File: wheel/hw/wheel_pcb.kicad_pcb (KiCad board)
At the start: 2 copper layers, 36 x 67 mm, 50 parts, among them J2 DEBUG, J3 IO_C, J4 CAR, J5 IO_B, J6 IO_A, SW1 CONFIG, U1 LPC11C24FBD48, U2 TPS62175, U3 TLV70233_SOT23-5, Y1 12MHz

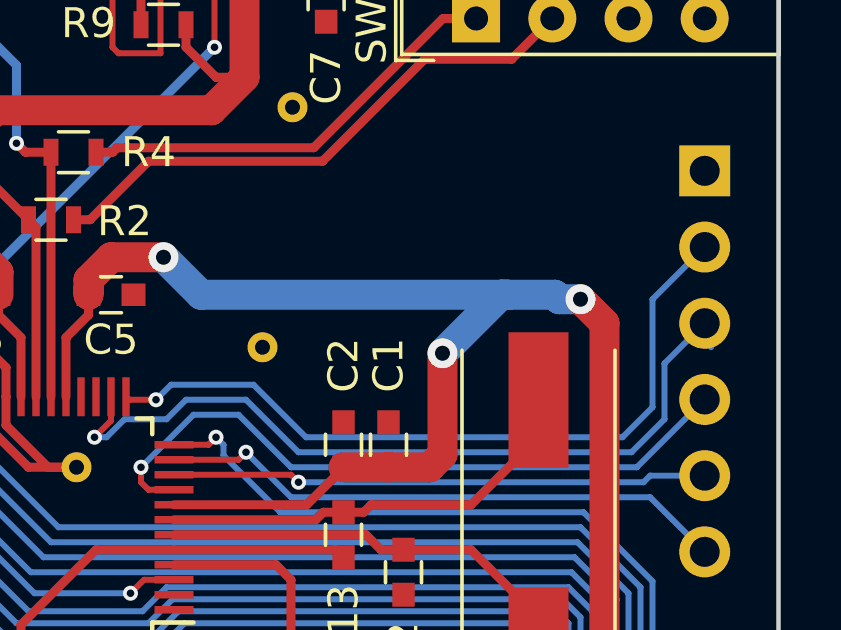
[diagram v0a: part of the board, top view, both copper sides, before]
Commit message: remove stray track and clean up tracks
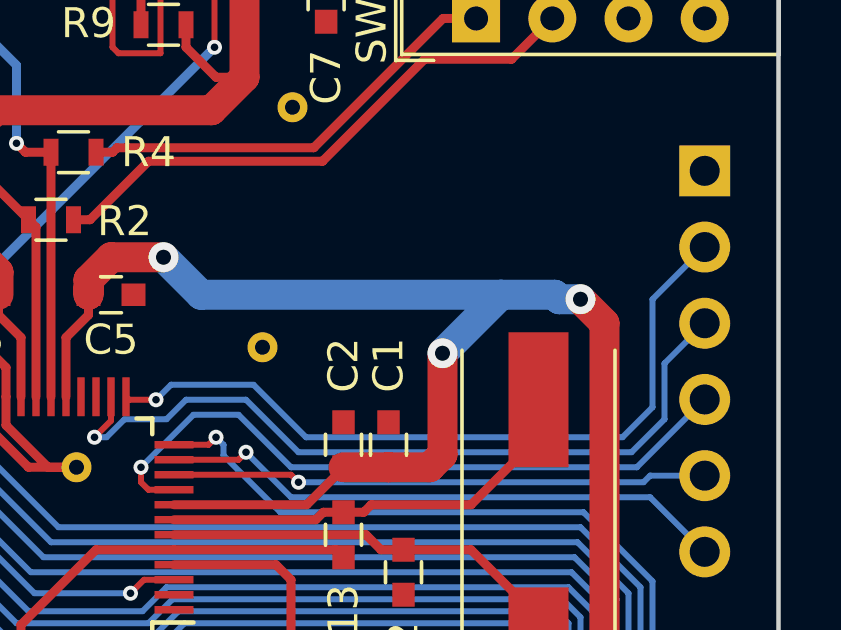
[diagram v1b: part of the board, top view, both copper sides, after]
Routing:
- net /IO_C2: track 26.9 -> 26.0 mm
- net +3V3: track 145.3 -> 144.8 mm
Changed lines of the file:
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@@
     (links 120)
     (no_connects 0)
-    (area 222.924999 54.924999 259.075001 122.075001)
+    (area 217.492857 54.924999 261.045 123.025)
     (thickness 1.6)
     (drawings 11)
-    (tracks 404)
+    (tracks 402)
     (zones 0)
     (modules 50)
@@
     (pcbplotparams
       (layerselection 0x010f0_80000001)
-      (usegerberextensions false)
+      (usegerberextensions true)
       (excludeedgelayer true)
       (linewidth 0.100000)
@@
       (drillshape 0)
       (scaleselection 1)
-      (outputdirectory ""))
+      (outputdirectory r1/))
   )
   (net 0 "")
@@
   (segment (start 247.8 80.575) (end 247.375 81) (width 1) (layer F.Cu) (net 3))
   (segment (start 247.8 77.2) (end 249.75 75.25) (width 1) (layer B.Cu) (net 3))
-  (segment (start 249.75 75.25) (end 250 75.25) (width 1) (layer B.Cu) (net 3))
+  (segment (start 249.75 75.25) (end 239.75 75.25) (width 1) (layer B.Cu) (net 3))
   (segment (start 245 96.15) (end 245 93) (width 1) (layer F.Cu) (net 3) (status 10))
   (segment (start 245 93) (end 242.75 90.75) (width 1) (layer F.Cu) (net 3))
@@
   (segment (start 236 75.25) (end 236 74.75) (width 1) (layer F.Cu) (net 3) (status 10))
   (segment (start 236 75) (end 236 75.25) (width 1) (layer F.Cu) (net 3) (status 30))
-  (segment (start 250 75.25) (end 239.75 75.25) (width 1) (layer B.Cu) (net 3))
   (segment (start 239.75 75.25) (end 238.5 74) (width 1) (layer B.Cu) (net 3))
   (via (at 238.5 74) (size 1) (drill 0.5) (layers F.Cu B.Cu) (net 3))
@@
   (segment (start 244.5 81) (end 244.5 80.975) (width 0.5) (layer F.Cu) (net 3) (status 30))
   (segment (start 242 90) (end 242.75 90.75) (width 1) (layer B.Cu) (net 3))
-  (segment (start 232.75 87.35) (end 232.75 88.3) (width 0.3) (layer F.Cu) (net 4))
+  (segment (start 232.75 87.35) (end 232.75 88.3) (width 0.3) (layer F.Cu) (net 4) (status 10))
   (segment (start 232.75 88.3) (end 232.45 88.6) (width 0.3) (layer F.Cu) (net 4))
   (segment (start 232.45 88.6) (end 231.4 88.6) (width 0.3) (layer F.Cu) (net 4))
@@
   (segment (start 230.2 88) (end 227.4 90.8) (width 0.3) (layer F.Cu) (net 4))
   (segment (start 227.4 90.8) (end 227.4 93.65) (width 0.3) (layer F.Cu) (net 4))
-  (segment (start 227.4 93.65) (end 226.6 94.45) (width 0.3) (layer F.Cu) (net 4))
-  (segment (start 226.6 94.45) (end 226.4 94.45) (width 0.3) (layer F.Cu) (net 4))
+  (segment (start 227.4 93.65) (end 226.6 94.45) (width 0.3) (layer F.Cu) (net 4) (status 20))
+  (segment (start 226.6 94.45) (end 226.4 94.45) (width 0.3) (layer F.Cu) (net 4) (status 30))
   (segment (start 226.4 93.8) (end 225.65 93.8) (width 0.3) (layer F.Cu) (net 5))
-  (segment (start 225.65 93.8) (end 225 94.45) (width 0.3) (layer F.Cu) (net 5))
-  (segment (start 225 94.45) (end 224.8 94.45) (width 0.3) (layer F.Cu) (net 5))
+  (segment (start 225.65 93.8) (end 225 94.45) (width 0.3) (layer F.Cu) (net 5) (status 20))
+  (segment (start 225 94.45) (end 224.8 94.45) (width 0.3) (layer F.Cu) (net 5) (status 30))
   (segment (start 226.8 93.4) (end 226.4 93.8) (width 0.3) (layer F.Cu) (net 5))
   (segment (start 226.8 90.4) (end 226.8 93.4) (width 0.3) (layer F.Cu) (net 5))
@@
   (via (at 237.4 85.2) (size 0.5) (drill 0.25) (layers F.Cu B.Cu) (net 37))
   (segment (start 247.2 67.4) (end 250.1 67.4) (width 0.3) (layer F.Cu) (net 38))
-  (segment (start 250.1 67.4) (end 251.46 66.04) (width 0.3) (layer F.Cu) (net 38))
+  (segment (start 250.1 67.4) (end 251.46 66.04) (width 0.3) (layer F.Cu) (net 38) (status 20))
   (segment (start 238 70.8) (end 243.8 70.8) (width 0.3) (layer F.Cu) (net 38))
   (segment (start 243.8 70.8) (end 247.2 67.4) (width 0.3) (layer F.Cu) (net 38))
   (segment (start 236.05 72.75) (end 238 70.8) (width 0.3) (layer F.Cu) (net 38))
-  (segment (start 235.5 72.75) (end 236.05 72.75) (width 0.3) (layer F.Cu) (net 38))
+  (segment (start 235.5 72.75) (end 236.05 72.75) (width 0.3) (layer F.Cu) (net 38) (status 10))
   (segment (start 235.5 72.75) (end 235.5 72.55) (width 0.3) (layer F.Cu) (net 38) (status 30))
-  (segment (start 247.82 66.04) (end 248.92 66.04) (width 0.3) (layer F.Cu) (net 39))
+  (segment (start 247.82 66.04) (end 248.92 66.04) (width 0.3) (layer F.Cu) (net 39) (status 20))
   (segment (start 243.510009 70.349991) (end 247.82 66.04) (width 0.3) (layer F.Cu) (net 39))
   (segment (start 236.950009 70.349991) (end 243.510009 70.349991) (width 0.3) (layer F.Cu) (net 39))
   (segment (start 236.8 70.5) (end 236.950009 70.349991) (width 0.3) (layer F.Cu) (net 39))
-  (segment (start 236.25 70.5) (end 236.8 70.5) (width 0.3) (layer F.Cu) (net 39))
+  (segment (start 236.25 70.5) (end 236.8 70.5) (width 0.3) (layer F.Cu) (net 39) (status 10))
   (segment (start 236.25 70.5) (end 236.25 70.7) (width 0.3) (layer F.Cu) (net 39) (status 30))
   (segment (start 238.25 78.75) (end 238.75 78.25) (width 0.2) (layer B.Cu) (net 44))
@@
   (segment (start 255.2 77.54) (end 256.54 76.2) (width 0.2) (layer B.Cu) (net 45) (status 20))
   (via (at 236.2 80) (size 0.5) (drill 0.25) (layers F.Cu B.Cu) (net 45))
-  (segment (start 256.75 77) (end 256.75 76.127919) (width 0.2) (layer B.Cu) (net 45) (status 30))
   (segment (start 237.75 81) (end 239.5 79.25) (width 0.2) (layer B.Cu) (net 46))
   (segment (start 239.5 79.25) (end 241 79.25) (width 0.2) (layer B.Cu) (net 46))

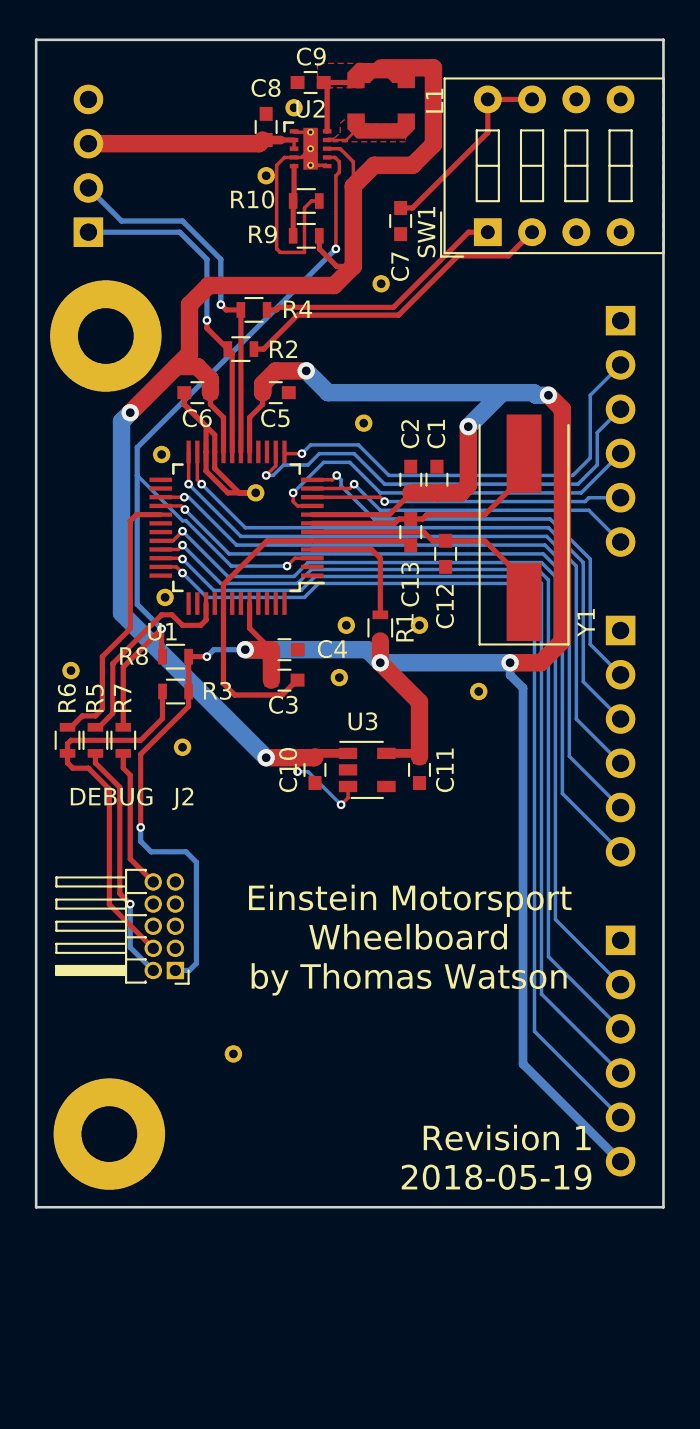
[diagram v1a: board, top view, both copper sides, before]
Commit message: draft layout of new wheel stuff
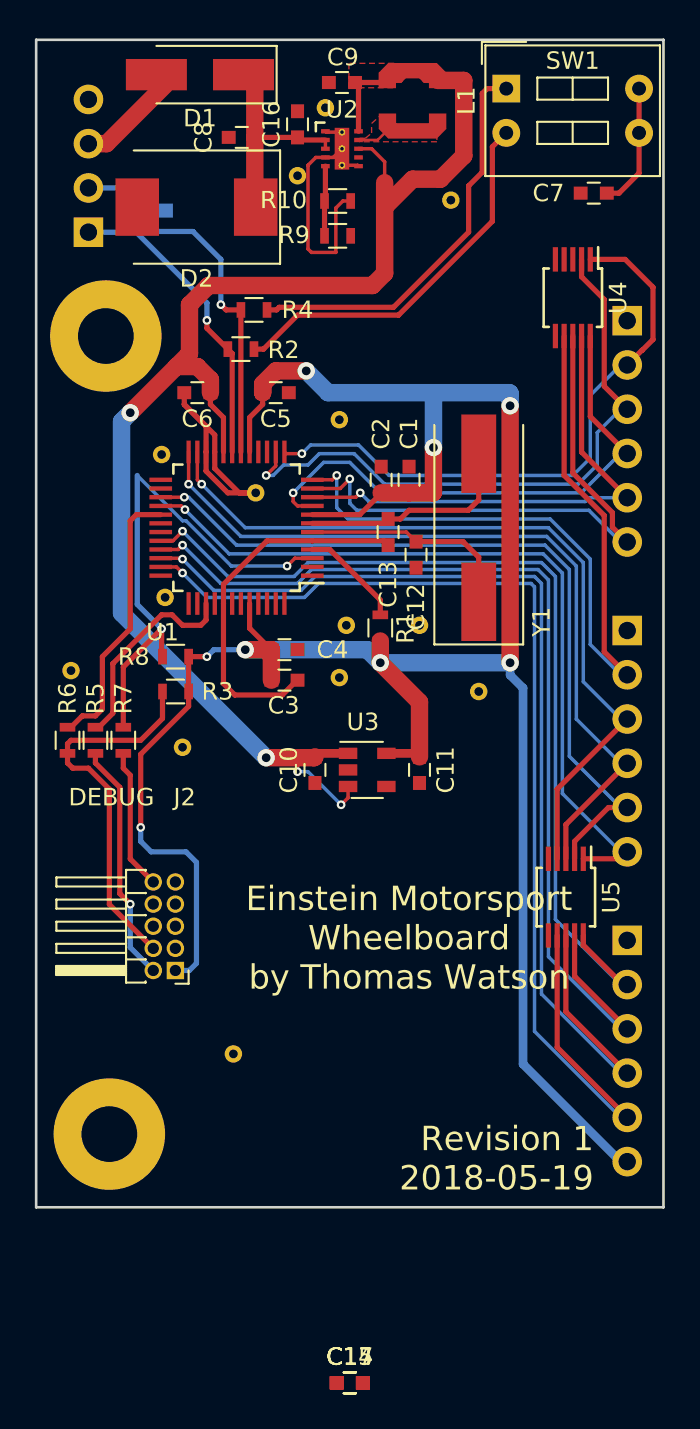
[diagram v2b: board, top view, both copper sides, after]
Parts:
- added C14, C15, C17: 100n, Capacitors_SMD:C_0603, F.Cu at (241.0, 132.1)
- added C16: 100n, Capacitors_SMD:C_0603, F.Cu at (238.0, 59.9)
- added D1: SS14, Diodes_SMD:D_SMA_Handsoldering, F.Cu at (232.4, 57.0)
- added D2: SMLJ22A-Q, Diodes_SMD:D_SMC, F.Cu at (232.2, 64.6)
- added D3: PESD1CAN-U, TO_SOT_Packages_SMD:SOT-23, B.Cu at (229.4, 64.8)
- added U4: SP4065-08ATG, Housings_SSOP:MSOP-10_3x3mm_Pitch0.5mm, F.Cu at (253.8, 69.8)
- added U5: SP4065-08ATG, Housings_SSOP:MSOP-10_3x3mm_Pitch0.5mm, F.Cu at (253.4, 104.2)
- R2, R4: value 60.4 -> 62
- R5, R6, R7: value 60.4 -> 100
- SW1: value CONFIG -> TERM; footprint Buttons_Switches_THT:SW_DIP_x4_W7.62mm_Slide -> Buttons_Switches_THT:SW_DIP_x2_W7.62mm_Slide
- moved C7 11.2 mm to (255.0, 63.8), turned to 180 degrees
- moved SW1 8.31 mm to (250.0, 57.8), turned to 0 degrees
- moved REF** 6.25 mm to (246.8, 64.2)
- moved Y1 2.60 mm to (248.4, 83.0)
- moved C9 1.80 mm to (240.6, 57.5)
- moved R10 1.80 mm to (240.3, 64.2)
- moved R9 1.80 mm to (240.3, 66.2)
- moved REF** 1.80 mm to (238.0, 62.8)
- moved U2 1.80 mm to (240.6, 61.2)
- moved L1 1.80 mm to (244.6, 58.5)
- moved REF** 1.80 mm to (239.6, 58.9)
- moved C12 1.70 mm to (244.8, 84.5)
- moved C2 1.70 mm to (242.8, 80.2)
- moved C1 1.60 mm to (244.4, 80.2)
- moved C8 1.52 mm to (234.8, 60.6), turned to 180 degrees
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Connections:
- C8 pad 1: +BATT -> Net-(C16-Pad1)
- SW1 pad 3: Net-(SW1-Pad3) -> Net-(C7-Pad1)
- SW1 pad 4: Net-(SW1-Pad4) -> Net-(C7-Pad1)
- U2 pad 2: +BATT -> Net-(C16-Pad1)
- U2 pad 3: +BATT -> Net-(C16-Pad1)
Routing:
- net /MCU_~RESET: track 53.6 -> 30.0 mm, vias 3 -> 2
- net /IO_B1: track 25.6 -> 47.4 mm
- net Net-(C16-Pad1): track 0.00 -> 14.5 mm
- net /IO_C5: track 19.2 -> 33.4 mm
- net /IO_A4: track 55.1 -> 67.2 mm
- net /IO_C4: track 17.9 -> 28.5 mm
- net /IO_C2: track 26.0 -> 35.7 mm
- net /IO_B2: track 35.6 -> 45.3 mm
- net /IO_A3: track 53.1 -> 62.5 mm
- net /IO_C1: track 25.0 -> 34.3 mm
- net /CANL_TERM: track 14.7 -> 23.4 mm
- net /IO_C3: track 22.9 -> 30.5 mm
- net +3V3: track 144.8 -> 137.5 mm
- net /IO_B3: track 38.4 -> 45.4 mm
- net /IO_A2: track 51.3 -> 57.9 mm
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
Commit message: rework some tracks
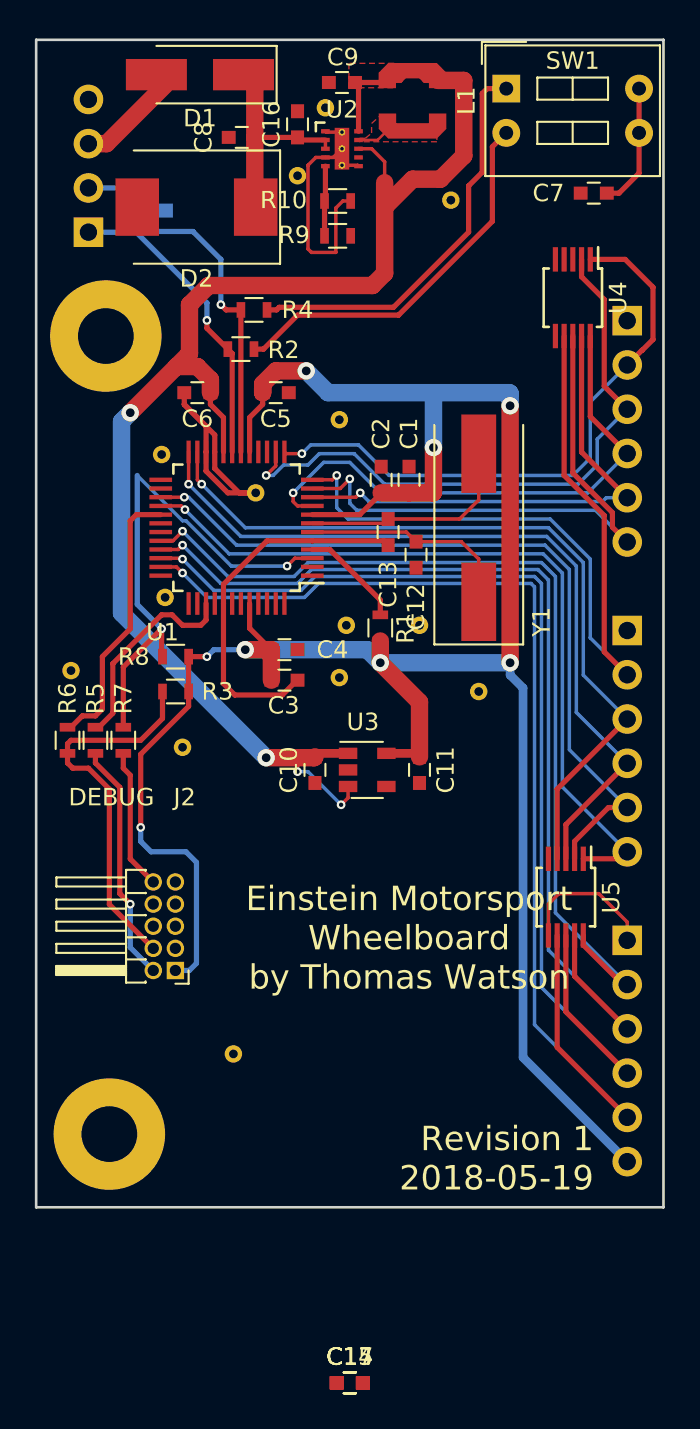
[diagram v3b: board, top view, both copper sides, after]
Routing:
- net GND: track 51.2 -> 59.5 mm

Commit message: pretty much finish wheel layout
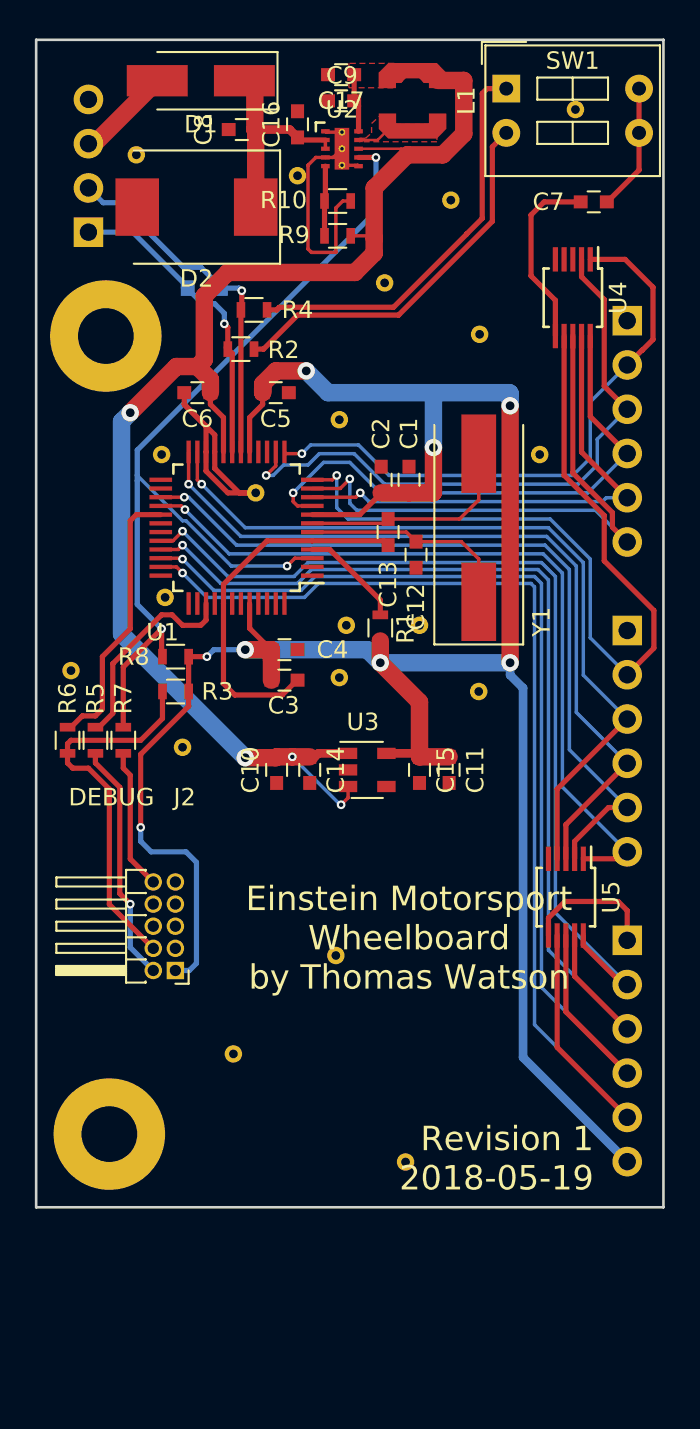
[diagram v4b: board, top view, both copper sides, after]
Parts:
- removed the REF** at (239.6, 58.9)
- added REF**: a_via, custom_footprints:a_via, B.Cu at (248.4, 71.9)
- added REF**: a_via, custom_footprints:a_via, B.Cu at (253.9, 59.0)
- added REF**: a_via, custom_footprints:a_via, B.Cu at (240.2, 107.5)
- added REF**: a_via, custom_footprints:a_via, B.Cu at (244.2, 119.4)
- added REF**: a_via, custom_footprints:a_via, F.Cu at (251.9, 78.8)
- added REF**: a_via, custom_footprints:a_via, F.Cu at (243.0, 69.0)
- added REF**: a_via, custom_footprints:a_via, F.Cu at (228.8, 61.6)
- moved C17 75.1 mm to (240.5, 57.0), turned to 180 degrees
- moved C15 35.4 mm to (245.0, 96.9), turned to 270 degrees
- moved C14 35.3 mm to (238.7, 96.9), turned to 270 degrees
- moved D3 6.35 mm to (232.7, 70.2), turned to 270 degrees
- moved C10 2.20 mm to (236.8, 96.9)
- moved C11 1.70 mm to (246.7, 96.9)
- moved C9 1.05 mm to (240.5, 58.5)
- moved C7 0.50 mm to (255.0, 64.3)
- moved C8 0.45 mm to (234.8, 60.1)
- moved D1 0.35 mm to (232.4, 57.4)
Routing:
- net /MCU_~RESET: track 30.0 -> 56.6 mm, vias 2 -> 3
- net GND: track 59.5 -> 69.7 mm
- net +5V: track 88.3 -> 85.8 mm
- net +3V3: track 137.7 -> 139.4 mm
- net /IO_B1: track 47.6 -> 48.9 mm
- net /CANL: track 21.7 -> 20.8 mm
- net Net-(C16-Pad1): track 14.5 -> 15.3 mm
